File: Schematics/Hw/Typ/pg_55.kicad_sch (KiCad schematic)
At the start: 16 parts, among them U5701 F194, U5702 F194, U5703 F194, U5704 F194, U5705 F194, U5706 F194, U5707 F04, U5708 F37, U5709 F37, U5710 F138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

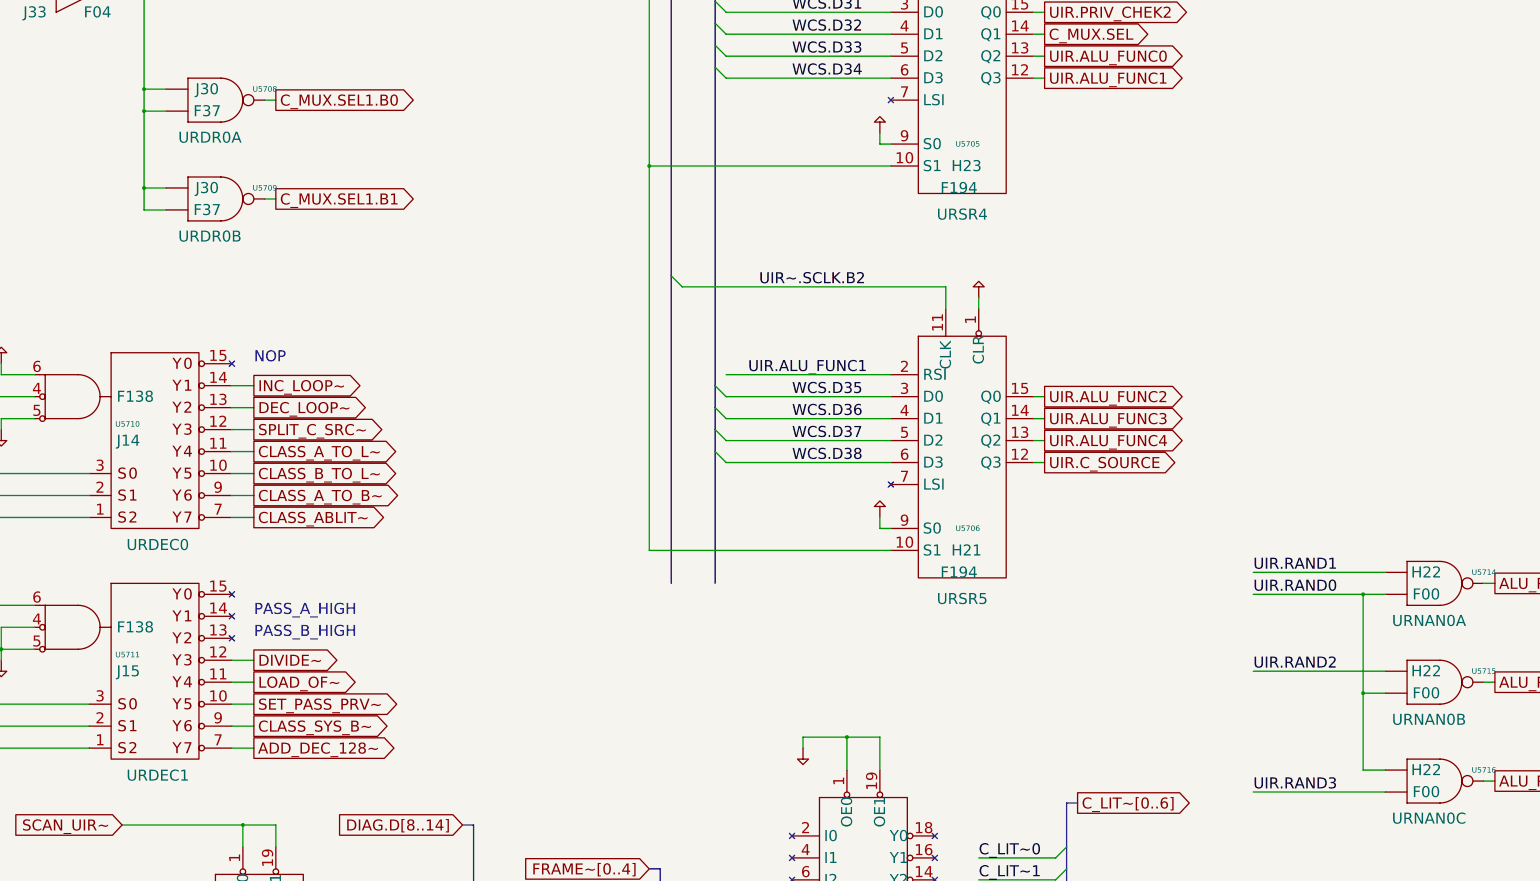
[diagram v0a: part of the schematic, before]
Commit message: Upgrade to KiCad9
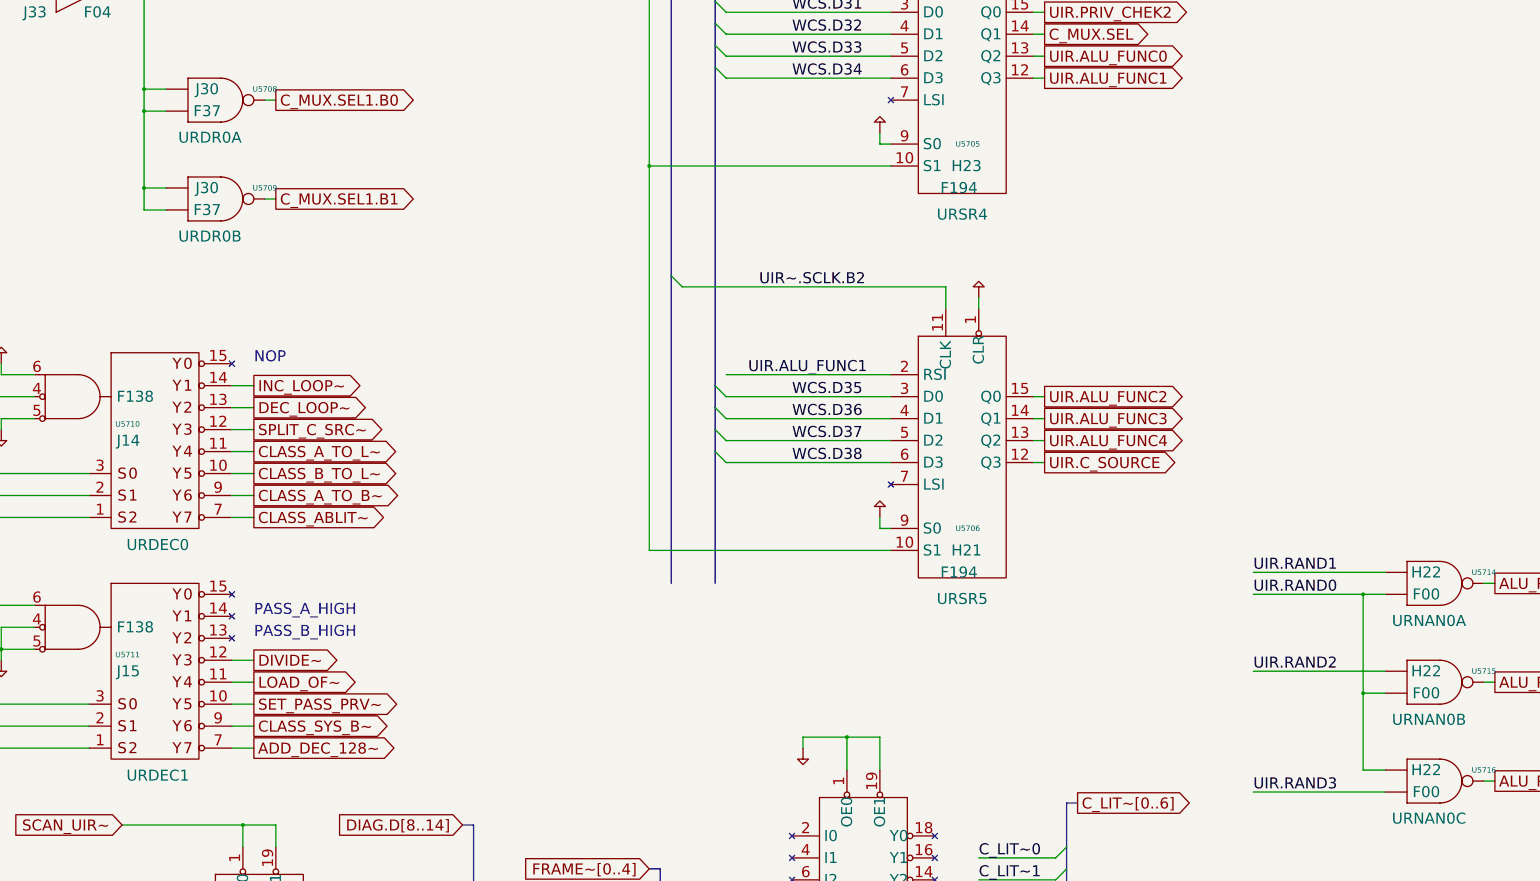
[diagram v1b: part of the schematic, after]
